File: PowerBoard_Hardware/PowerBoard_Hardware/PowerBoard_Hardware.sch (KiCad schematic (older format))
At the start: 81 parts

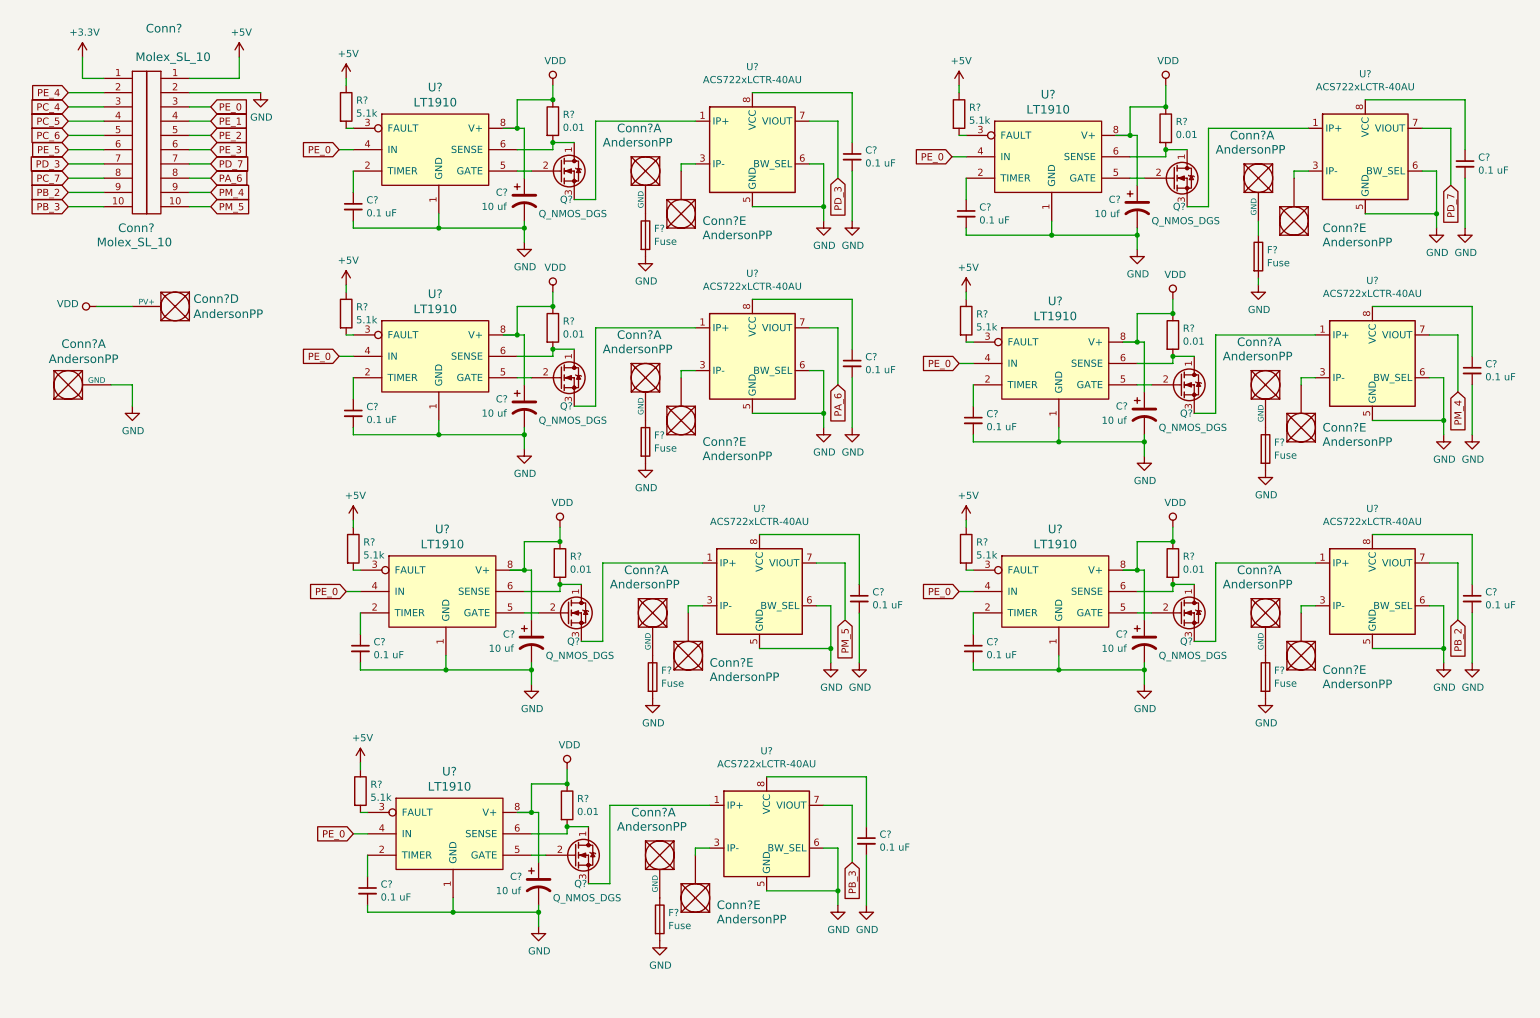
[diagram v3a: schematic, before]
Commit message: Pass 1.5
*pvv changed to PVDD
*Fuses placed before each anderson
*pcb layout generated
*PVDD via has issues
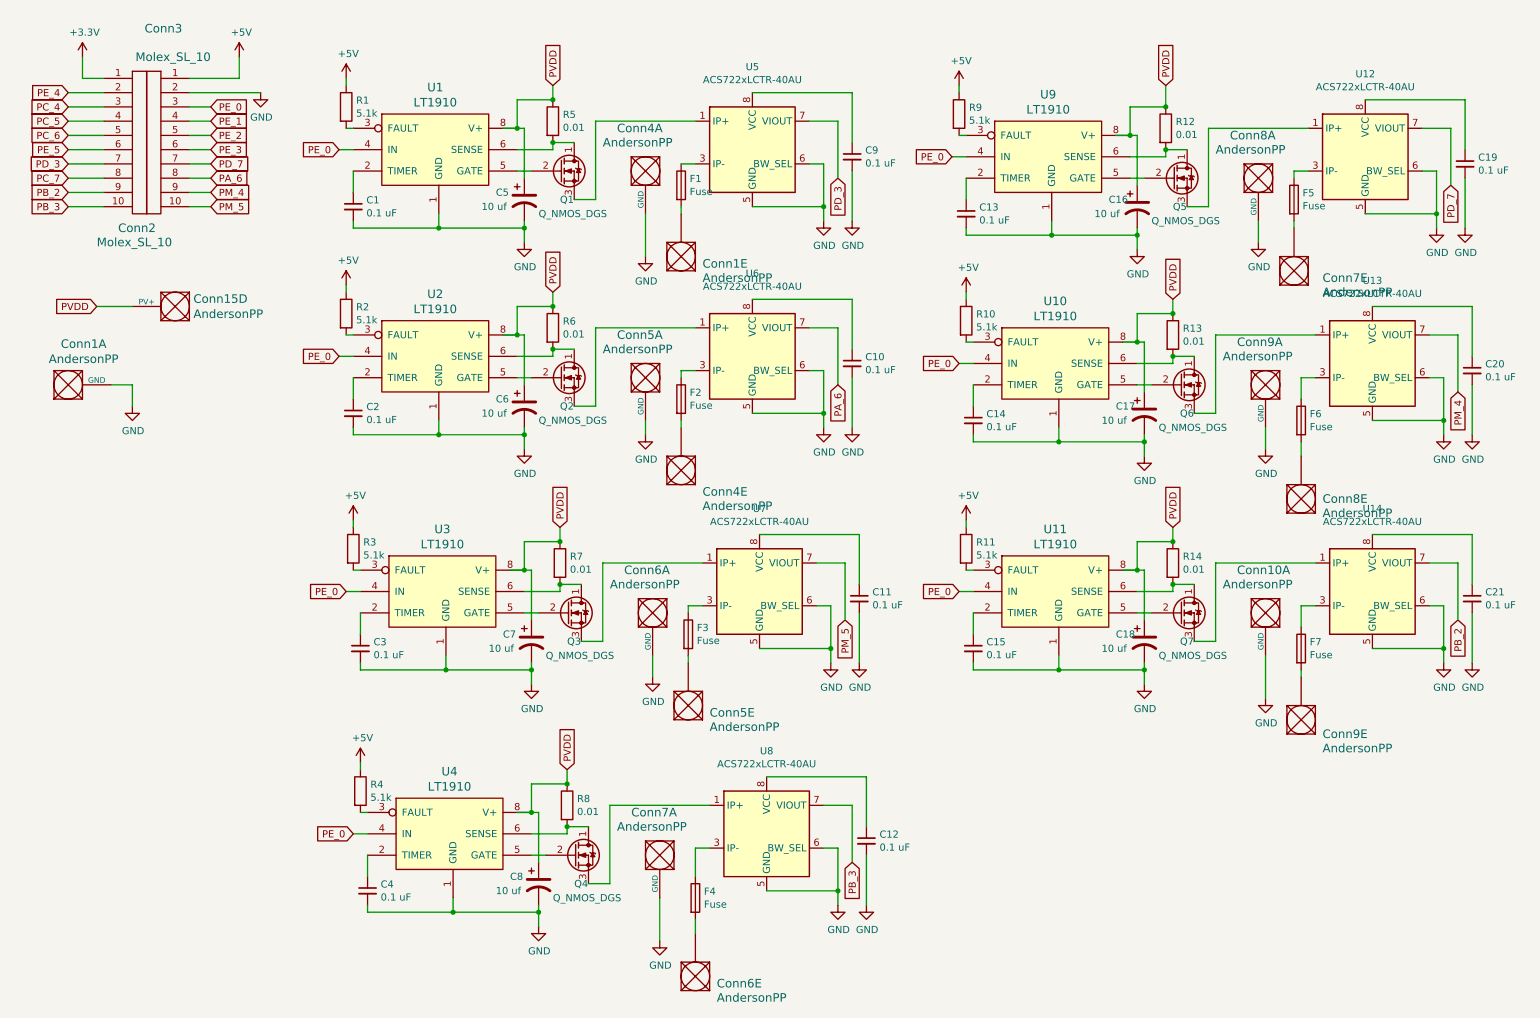
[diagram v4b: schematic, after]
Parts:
- removed F?: Fuse, symbol Device:Fuse
- added F1: Fuse, MRDT_Passives:ATC_Fuse_Block, symbol Device:Fuse
- C1, C10, C11, C12, C13, C14, C15, C16, C17, C18, C19, C2, C20, C21, C3, C4, C5, C6, C7, C8, C9: renamed from C?; footprint (none) -> Capacitor_SMD:C_0603_1608Metric_Pad1.05x0.95mm_HandSolder
- Conn1, Conn15: renamed from Conn?; footprint (none) -> MRDT_Drill_Holes:BATT_PWR_VIA
- Conn10, Conn4, Conn5, Conn6, Conn7, Conn8, Conn9: renamed from Conn?; footprint (none) -> MRDT_Connectors:Anderson_2_Horizontal_Stacked
- Conn2, Conn3: renamed from Conn?; footprint (none) -> MRDT_Connectors:MOLEX_SL_10_Horizontal
- F2, F3, F4, F5, F6, F7: renamed from F?; footprint (none) -> MRDT_Passives:ATC_Fuse_Block
- Q1, Q2, Q3, Q4, Q5, Q6, Q7: renamed from Q?; footprint (none) -> Package_TO_SOT_SMD:TO-263-2
- R1, R10, R11, R12, R13, R14, R2, R3, R4, R5, R6, R7, R8, R9: renamed from R?; footprint (none) -> Resistor_SMD:R_0603_1608Metric_Pad1.05x0.95mm_HandSolder
- U1, U10, U11, U2, U3, U4, U9: renamed from U?; footprint (none) -> Package_SO:SOIC-8-N7_3.9x4.9mm_P1.27mm
- gave numbers to parts that had none: 7
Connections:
- net GND: now also Conn10.1 (GND), Conn4.1 (GND), Conn5.1 (GND), Conn6.1 (GND), Conn7.1 (GND), Conn8.1 (GND), Conn9.1 (GND); no longer F2.2, F3.2, F4.2, F5.2, F6.2, F7.2
- net at U5.3 (IP-), U5.4 (IP-): now also F1.1; no longer Conn1.1
- net at F5.1: now also U12.3 (IP-), U12.4 (IP-); no longer Conn8.1 (GND)
- net at U6.3 (IP-), U6.4 (IP-): now also F2.1; no longer Conn4.1
- net at U13.3 (IP-), U13.4 (IP-): now also F6.1; no longer Conn8.1
- net at U7.3 (IP-), U7.4 (IP-): now also F3.1; no longer Conn5.1
- net at U14.3 (IP-), U14.4 (IP-): now also F7.1; no longer Conn9.1
- net at U8.3 (IP-), U8.4 (IP-): now also F4.1; no longer Conn6.1
- net VDD renamed PVDD
- new net: Conn7.1, F5.2
- new net: Conn1.1, F1.2
- new net: Conn4.1, F2.2
- new net: Conn8.1, F6.2
- new net: Conn9.1, F7.2
- new net: Conn5.1, F3.2
- new net: Conn6.1, F4.2
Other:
- moved on the sheet: Conn1E, Conn4E, Conn5E, Conn6E, Conn7E, Conn8E, Conn9E, F2, F3, F4, F5, F6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

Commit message: Pass 1.6
*Pins were rearranged on the schematic appropriately
*Layout has been cleaned up and generalized for PDR
*Problems still persist with Conn15-PVDD
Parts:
- Conn2, Conn3: footprint MRDT_Connectors:MOLEX_SL_10_Horizontal -> MRDT_Connectors:MOLEX_SL_10_Vertical
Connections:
- net PC_4: now also U11.4 (IN)
- net PC_5: now also U4.4 (IN)
- net PE_0: no longer U10.4 (IN), U11.4 (IN), U2.4 (IN), U3.4 (IN), U4.4 (IN), U9.4 (IN)
- net PE_1: now also U9.4 (IN)
- net PE_2: now also U2.4 (IN)
- net PE_3: now also U10.4 (IN)
- net PE_4: now also U3.4 (IN)
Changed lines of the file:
@@
 F 0 "Conn2" H 1250 2050 60  0000 L CNN
 F 1 "Molex_SL_10" H 1100 1950 60  0000 L CNN
-F 2 "MRDT_Connectors:MOLEX_SL_10_Horizontal" H 1350 2650 60  0001 C CNN
+F 2 "MRDT_Connectors:MOLEX_SL_10_Vertical" H 1350 2650 60  0001 C CNN
 F 3 "" H 1350 2650 60  0001 C CNN
 	1    1350 2150
@@
 F 0 "Conn3" H 1400 3450 60  0000 L CNN
 F 1 "Molex_SL_10" H 1200 3250 60  0000 L CNN
-F 2 "MRDT_Connectors:MOLEX_SL_10_Horizontal" H 1550 2650 60  0001 C CNN
+F 2 "MRDT_Connectors:MOLEX_SL_10_Vertical" H 1550 2650 60  0001 C CNN
 F 3 "" H 1550 2650 60  0001 C CNN
 	1    1550 2150
@@
 $EndComp
 Text GLabel 2800 3150 0    50   Input ~ 0
-PE_0
+PE_2
 $Comp
 L Device:C_Small C2
@@
 $EndComp
 Text GLabel 7100 1750 0    50   Input ~ 0
-PE_0
+PE_1
 $Comp
 L Device:C_Small C13
@@
 $EndComp
 Text GLabel 7150 3200 0    50   Input ~ 0
-PE_0
+PE_3
 $Comp
 L Device:C_Small C14
@@
 $EndComp
 Text GLabel 2850 4800 0    50   Input ~ 0
-PE_0
+PE_4
 $Comp
 L Device:C_Small C3
@@
 $EndComp
 Text GLabel 7150 4800 0    50   Input ~ 0
-PE_0
+PC_4
 $Comp
 L Device:C_Small C15
@@
 $EndComp
 Text GLabel 2900 6500 0    50   Input ~ 0
-PE_0
+PC_5
 $Comp
 L Device:C_Small C4

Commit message: Pass 1.7
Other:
- note added: "LAYOUT:\n*Make the layout increase the vertical dimension \nand decrease the horizintal dimentions \n(to condense the design and eliminate wasted space)\n*Move the GND and the Vin vias apart from \neach other on the layout\n*Ground the frame of the layout\n \nSCHEMATIC: \n*Add LEDs or some sort of indicator to the schematic\n*Protection diodes should be added for the MOSFETs\n\n"
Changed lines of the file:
@@
 Text GLabel 4400 6050 1    50   Input ~ 0
 PVDD
+Text Notes 500  5250 0    50   ~ 0
+LAYOUT:\n*Make the layout increase the vertical dimension \nand decrease the horizintal dimentions \n(to condense the design and eliminate wasted space)\n*Move the GND and the Vin vias apart from \neach other on the layout\n*Ground the frame of the layout\n \nSCHEMATIC: \n*Add LEDs or some sort of indicator to the schematic\n*Protection diodes should be added for the MOSFETs\n\n
 $EndSCHEMATC
